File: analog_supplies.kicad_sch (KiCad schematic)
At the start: 33 parts, among them Q1 PMOS, Q4 2NPN, U24 LDO-ADJ

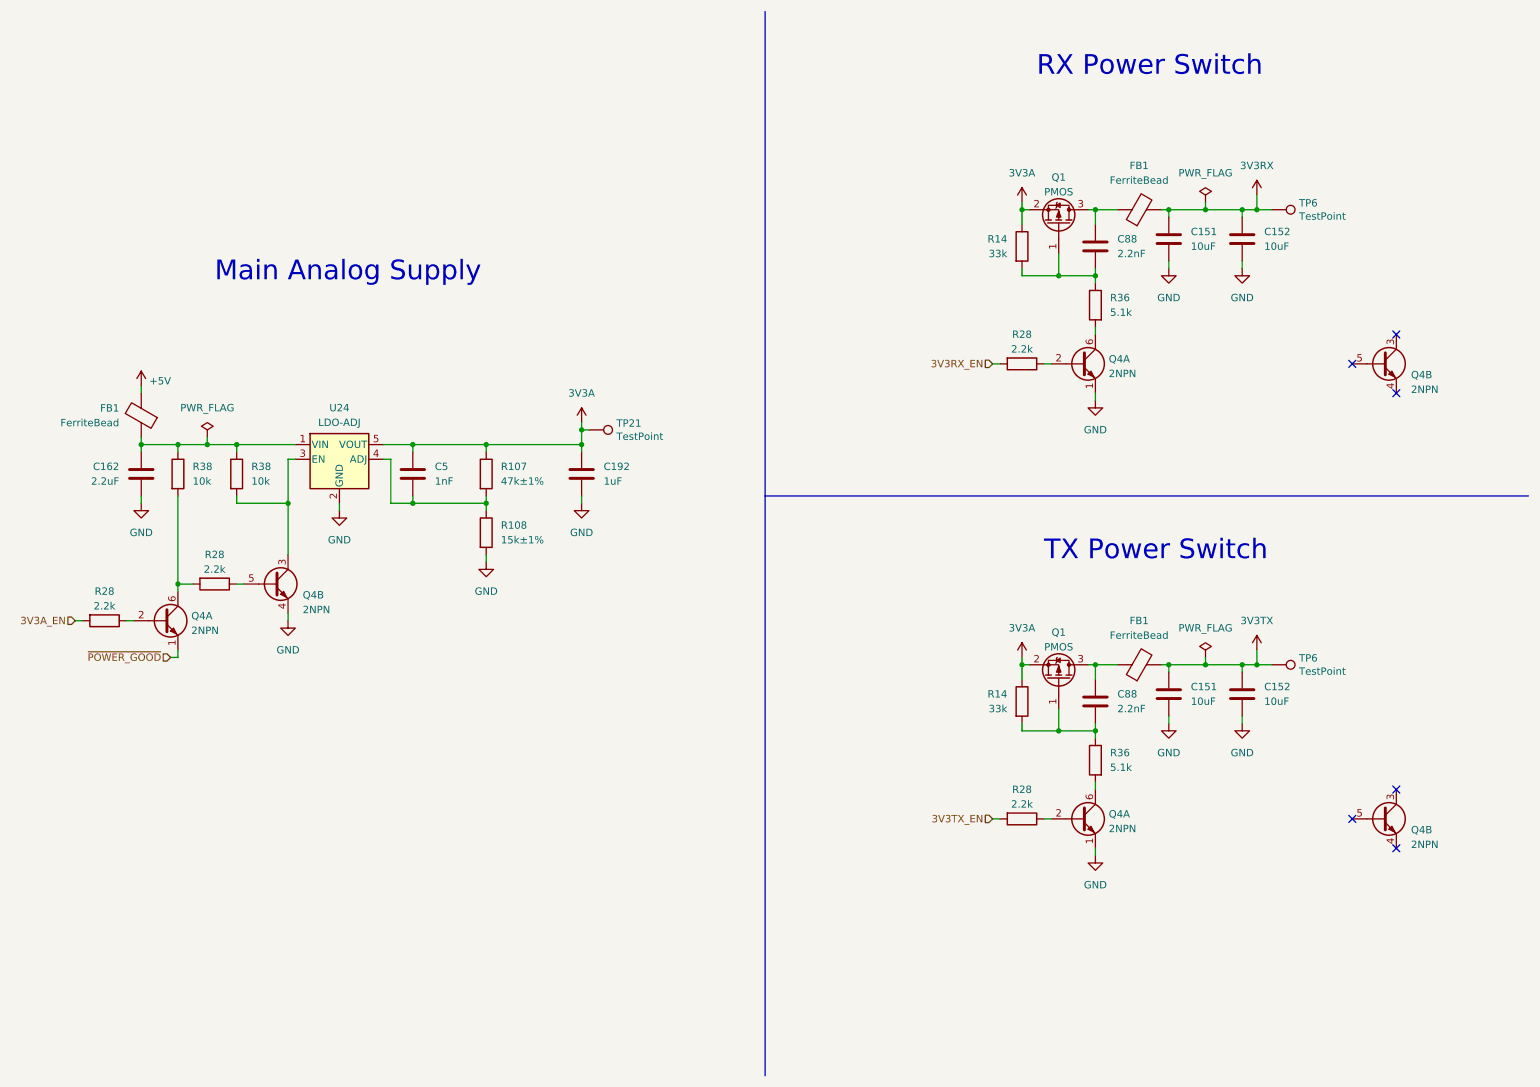
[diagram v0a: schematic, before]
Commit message: Replace open drain clock inverters with push-pull
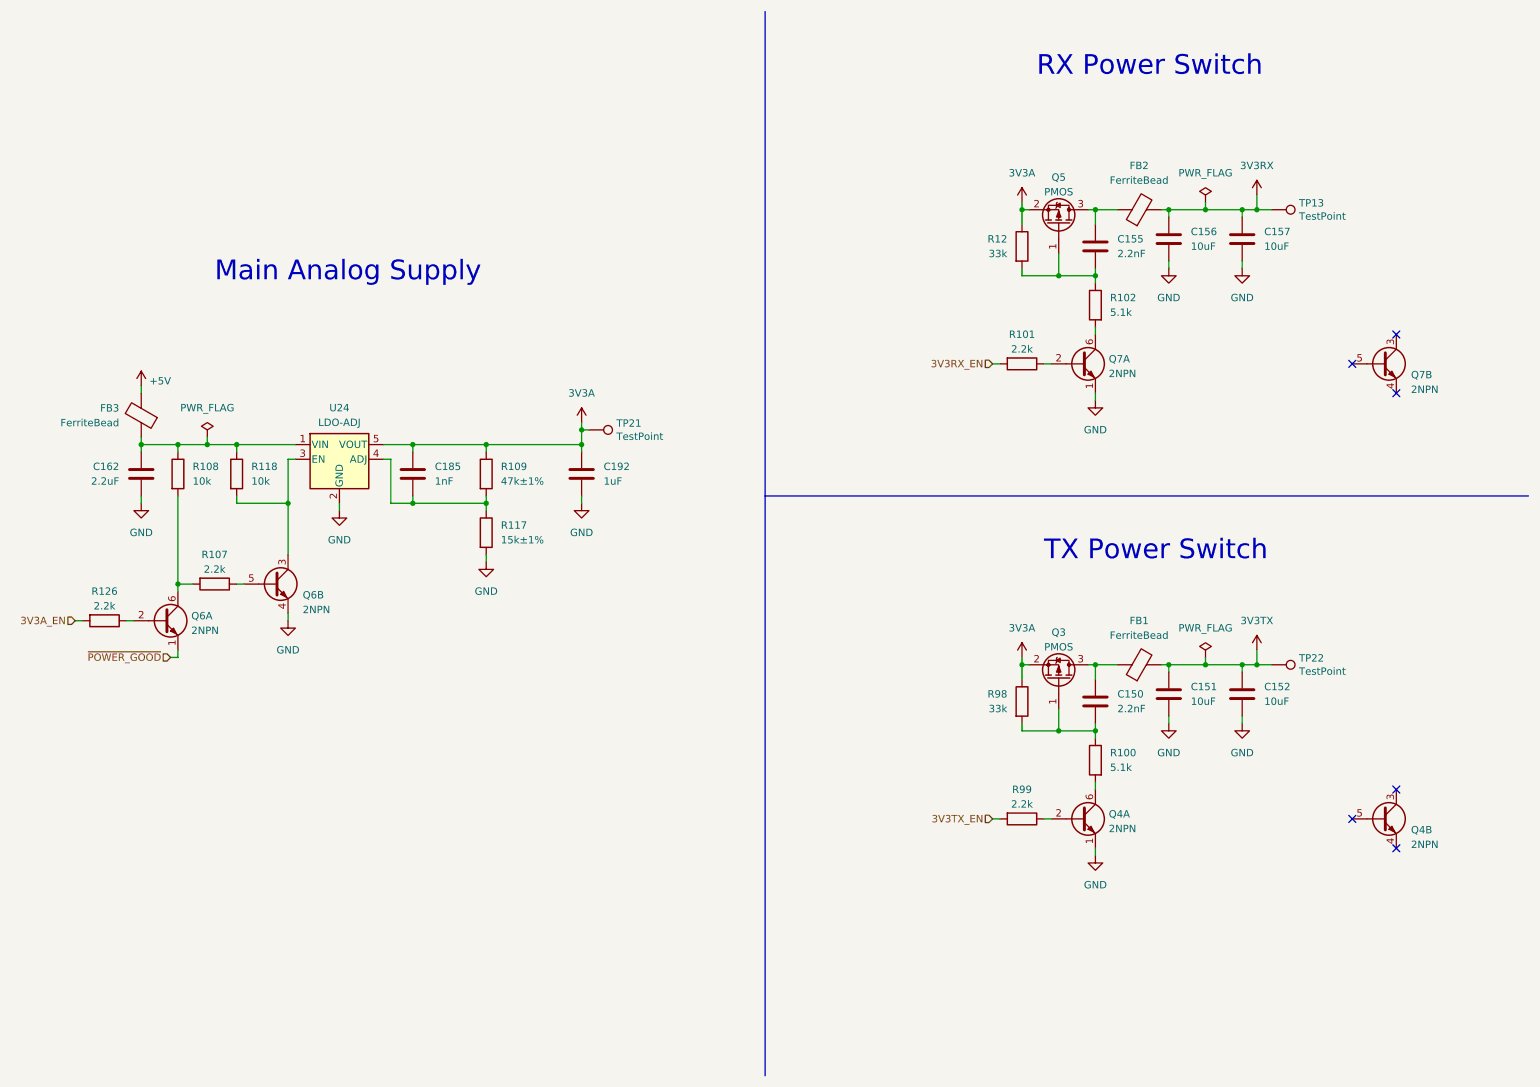
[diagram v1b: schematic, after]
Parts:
- renumbered C88 to C150, C88 to C155, C151 to C156, C152 to C157, C5 to C185, FB1 to FB2, FB1 to FB3, Q1 to Q3, Q1 to Q5, Q4 to Q6, Q4 to Q7, R36 to R100, R28 to R101, R36 to R102, R28 to R107, R38 to R108, R107 to R109, R108 to R117, R38 to R118, R14 to R12, R28 to R126, R14 to R98, R28 to R99, TP6 to TP13, TP6 to TP22

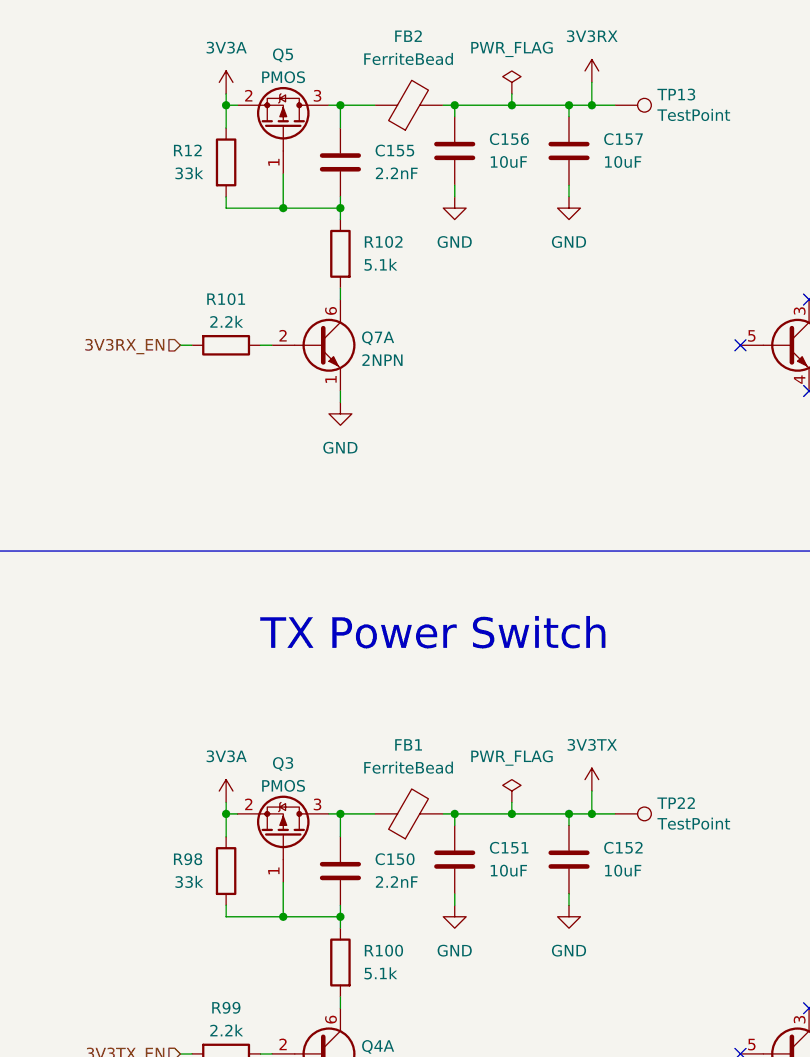
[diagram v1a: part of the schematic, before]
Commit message: Tune slow-start capacitors
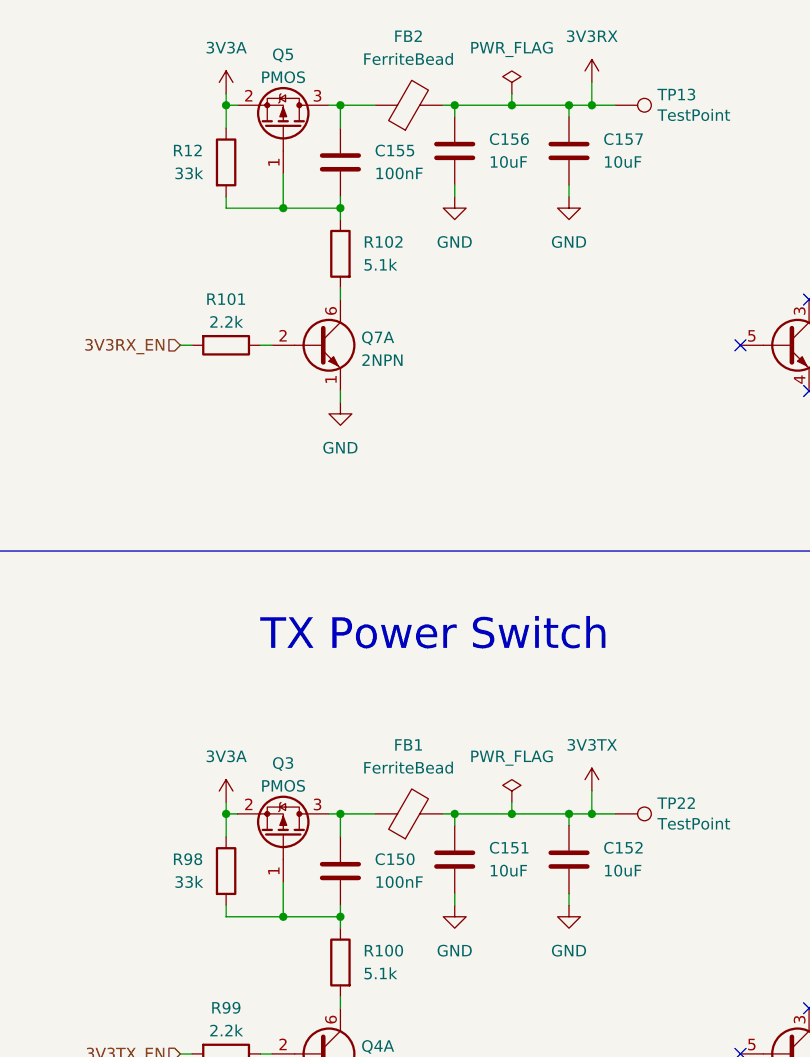
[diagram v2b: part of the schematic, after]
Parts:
- C150, C155: value 2.2nF -> 100nF; Part Number GRM033R71A222KA01D -> GRM033R61A104KE15D; Substitution GRM033R71A222KA01* -> GRM033R61A104KE15*
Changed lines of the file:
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@@
       (effects (font (size 1.27 1.27)) (justify right))
     )
-    (property "Value" "2.2nF" (at 213.36 133.35 0)
+    (property "Value" "100nF" (at 213.36 133.35 0)
       (effects (font (size 1.27 1.27)) (justify right))
     )
@@
       (effects (font (size 1.27 1.27)) hide)
     )
-    (property "Description" "CAP CER 2200PF 10V X7R 0201" (at 209.55 132.08 0)
+    (property "Description" "CAP CER 0.1UF 10V X5R 0201" (at 209.55 132.08 0)
       (effects (font (size 1.27 1.27)) hide)
     )
@@
       (effects (font (size 1.27 1.27)) hide)
     )
-    (property "Part Number" "GRM033R71A222KA01D" (at 209.55 132.08 0)
-      (effects (font (size 1.27 1.27)) hide)
-    )
-    (property "Substitution" "GRM033R71A222KA01*" (at 209.55 132.08 0)
+    (property "Part Number" "GRM033R61A104KE15D" (at 209.55 132.08 0)
+      (effects (font (size 1.27 1.27)) hide)
+    )
+    (property "Substitution" "GRM033R61A104KE15*" (at 209.55 132.08 0)
       (effects (font (size 1.27 1.27)) hide)
     )
@@
       (effects (font (size 1.27 1.27)) (justify right))
     )
-    (property "Value" "2.2nF" (at 213.36 54.61 0)
+    (property "Value" "100nF" (at 213.36 54.61 0)
       (effects (font (size 1.27 1.27)) (justify right))
     )
@@
       (effects (font (size 1.27 1.27)) hide)
     )
-    (property "Description" "CAP CER 2200PF 10V X7R 0201" (at 209.55 53.34 0)
+    (property "Description" "CAP CER 0.1UF 10V X5R 0201" (at 209.55 53.34 0)
       (effects (font (size 1.27 1.27)) hide)
     )
@@
       (effects (font (size 1.27 1.27)) hide)
     )
-    (property "Part Number" "GRM033R71A222KA01D" (at 209.55 53.34 0)
-      (effects (font (size 1.27 1.27)) hide)
-    )
-    (property "Substitution" "GRM033R71A222KA01*" (at 209.55 53.34 0)
-      (effects (font (size 1.27 1.27)) hide)
-    )
+    (property "Part Number" "GRM033R61A104KE15D" (at 209.55 53.34 0)
+      (effects (font (size 1.27 1.27)) hide)
+    )
+    (property "Substitution" "GRM033R61A104KE15*" (at 209.55 53.34 0)
+      (effects (font (size 1.27 1.27)) hide)
+    )
